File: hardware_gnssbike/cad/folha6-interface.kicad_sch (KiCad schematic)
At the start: 22 parts, among them Q601 DMG1012T-7, Q602 DMG1012T-7, Q603 DMG1012T-7, SW601 Omron B3S-1002P, SW602 Omron B3S-1002P, SW603 Omron B3S-1002P

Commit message: feat(hardware): the test points, a readable silkscreen, and paper that fits
Eleven of the sixteen test points of 06-conectores-e-pontos-de-teste.md were
not on the board. Only the three of the console sheet existed; a rail you
cannot put a probe on is a rail you cannot debug. VBUS, VBUSOUT, VBAT, VSYS,
3V0, 1V8, SD3V0, 3V3BL, VBCKP, VINT and the ground reference are there now,
each beside the thing it measures, and each takes what is LEFT: placed with
the rest of JUNTO they pushed three decoupling capacitors off their rings,
one of them to 4.0 mm from a pin that wants 2. The two that are still
missing are the document's own absences - TP111 measures ST_STO, which the
AEM10900 datasheet does not have, and TP401 measures 5V0, from a regulator
not fitted with the JDI panel. The list lives in parts.TESTE and nets.py
refuses a point that names a net that does not exist.

The silkscreen named nothing. Every reference sat 1.8 mm above its part at
0.7 mm with a 0.1 mm stroke - below the floor every fab publishes - and 37
pairs of designators printed on top of each other. The text is at the fab
minimum now, 0.8 mm with 0.15, and each label is PLACED: candidates around
its own courtyard, nearest first, never over another label and preferably
not over another part's outline. 127 references, 0 overlapping. The mounting
hole's REF** is hidden; it names nothing and was the last label sitting on
another.

Ground: a mesh, not just a hem. Edge stitching keeps the boundary of the
surface pours from becoming a radiating slot and does nothing for the
middle, where a patch of pour that reaches the inner plane through a via
20 mm away is not ground at 2.4 GHz. A 4.0 mm grid of ground vias now
covers the board - under the 6.1 mm that is a tenth of a wavelength in
FR-4 - laid last, on what is free, so a stitch never costs a connection.

The router's search learned about pad fields. The neck beside a pad existed
only in emitir(), and emitir only ever sees paths the search already found,
so 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
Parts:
- LS601: footprint Buzzer_Beeper:Buzzer_CUI_CPT-9019S-SMT -> gnssbike:Buzzer_CPT-1117-83-SMT_11x9mm
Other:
- moved on the sheet: C601, C602, C603, LS601, Q601, Q602, Q603, R601, R602, R603, R604, R605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

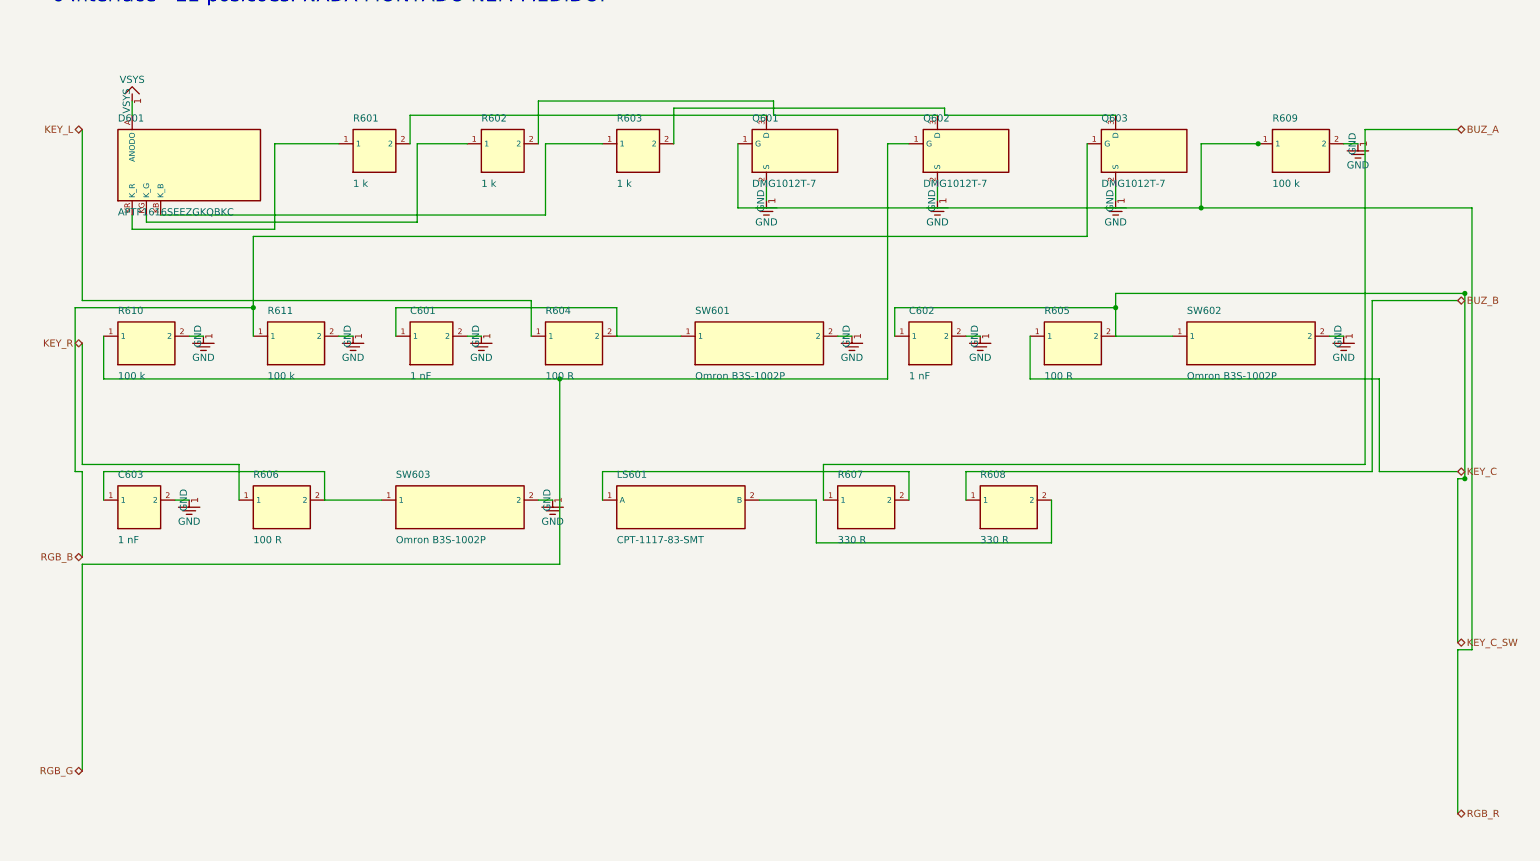
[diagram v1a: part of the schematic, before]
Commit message: feat(hardware): draw each part as its own symbol, not as a block
A rectangle with pin names down its sides is how an INTEGRATED CIRCUIT is
drawn, and only an integrated circuit. This generator drew all 127 parts
that way - resistors, ceramic capacitors, diodes, the TVS - and a sheet of
blocks joined by lines does not show a circuit.

Every class has its own symbol now, in the standard form, with the lead
axis on x and the body between -1.27 and +1.27 mm: a zigzag for a resistor
and a 0 ohm link (42 of them), two parallel plates for a ceramic capacitor
and a curved plate with a + for an electrolytic (31), four arcs for an
inductor (4), the same arcs inside a rectangle for a ferrite bead, which is
what tells the two apart, a zigzag with a diagonal arrow for the thermistor,
a triangle and a bar for a diode with arrows leaving it for an LED, two
contacts with a bar and a plunger for a key, a circle with a diagonal for
the buzzer, and a circle on the end of a lead for a test point. The 36 that
stay rectangles are the ones that should be: the ICs, the connectors and the
display. A two terminal part no longer prints pin numbers or pin names -
"1" and "2" on a resistor is noise, and the symbol already says which end is
which where it matters.

The power symbols had room reserved for the symbol and none for its NAME:
two ground pins two grid steps apart each got their own symbol, the symbols
did not collide, and the words printed over each other - "GNDGNDGND" along
the bottom of every chip. What is reserved now is the whole thing. With a
limit: the first cut let the stub run to fourteen grid steps looking for a
clear spot, and one of them crossed a component and split a net. A long stub
is worse than a crowded label, so it stops at eight and the label gives way.

One attempt is NOT in this commit, on purpose. Grouping every pin of a rail
on one edge into a single symbol - which is what a person draws - joins the
stubs with a line that runs along the part's edge and crosses w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
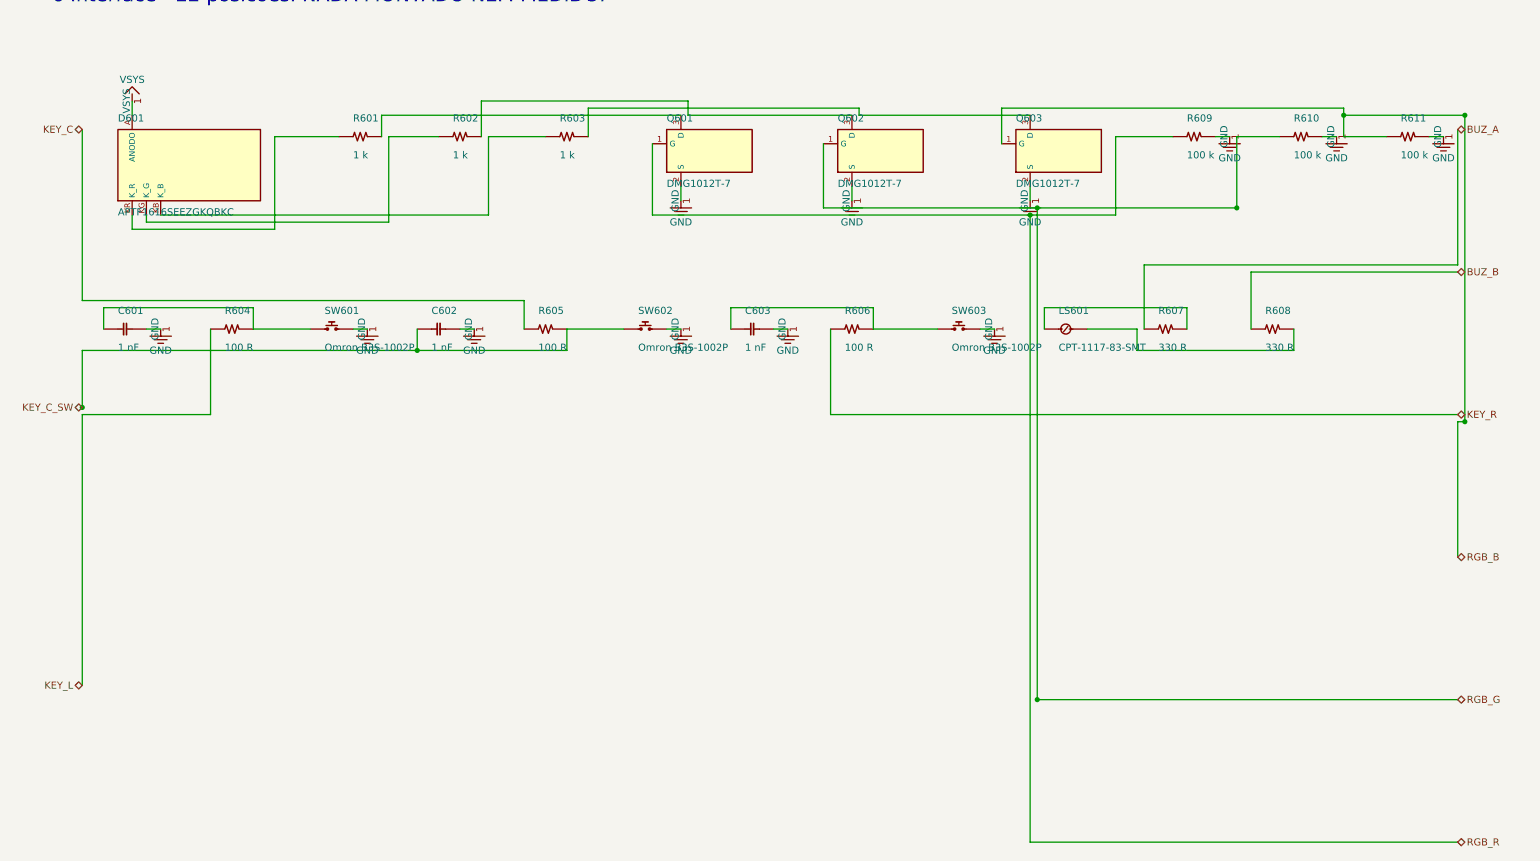
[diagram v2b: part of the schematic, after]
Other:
- moved on the sheet: Q601, Q602, Q603

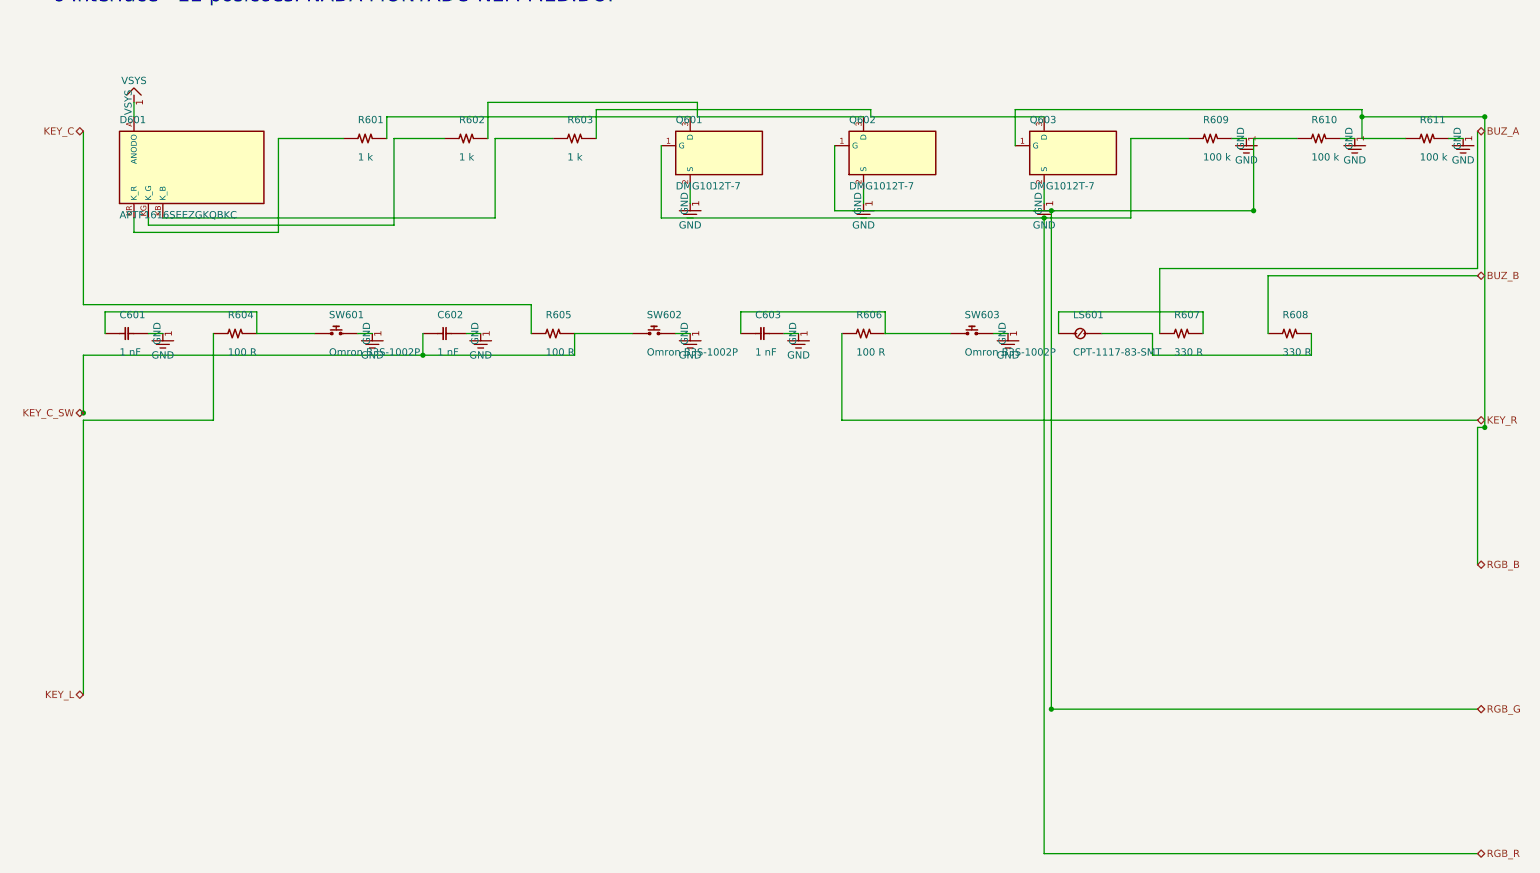
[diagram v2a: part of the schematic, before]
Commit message: feat(hardware): the four parts LCSC forced out, drawn from their drawings
The switch, the buzzer, the RGB LED and the magnetometer all had to
change, and each one came back from its drawing with something the
catalogue does not say.

  SW601..603  Omron B3S-1002P -> XunPu TS-1088R-02026 (C455280). It has
        TWO terminals, not four, so the land pattern is new even though
        the schematic already treated the key as two ends. Body 3,90 x
        3,00 x 2,00 against 6,6 x 6 x 3,4, which frees half the area the
        three keys took on the edge, and 260 gf against 230 - firmer,
        which is what gloves want. But the plunger rises only 0,50 mm
        above the steel cap against the Omron's 0,7, and the keys are
        pressed through the case: the case plunger changes.

  LS601  Same Sky CPT-1117-83-SMT (ONE in stock) -> Murata
        PKLCS1212E4001-R1 (C113159), the only substitute that keeps the
        84 dB. At 25 km/h with wind, the 65 to 70 dB of the 9 x 9 parts
        is inaudible, and an inaudible buzzer is no buzzer. The drawing
        corrects two things the catalogue hides: the sound hole is a
        LATERAL slot of 1,9 x 0,9 mm whose lower edge sits 0,30 mm off
        the board, with a channel underneath leaving by the opposite
        wall - so the case needs a side duct, not a hole in the lid -
        and the body is uniform dark graphite, with gold terminals, not
        black with a pale top. It also asks for 1 k to 2 k in series and
        forbids DC, which R607 and R608 now have to be checked against.

  D601  Kingbright APTF1616 (the suffix no longer exists, and what does
        has 305 pieces) -> TUOZHAN S4-3528RGBTA-A (C2827321), 2 million
        in stock at a twentieth of the price, common anode as the design
        wants. It is 3,5 x 2,8 instead of 1,6 x 1,6, so the LED zone had
        to widen and the part moved down 0,6 mm: at 1,9 mm tall it stood
        3,25 mm from the light sensor, which asks for twice a
        ne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
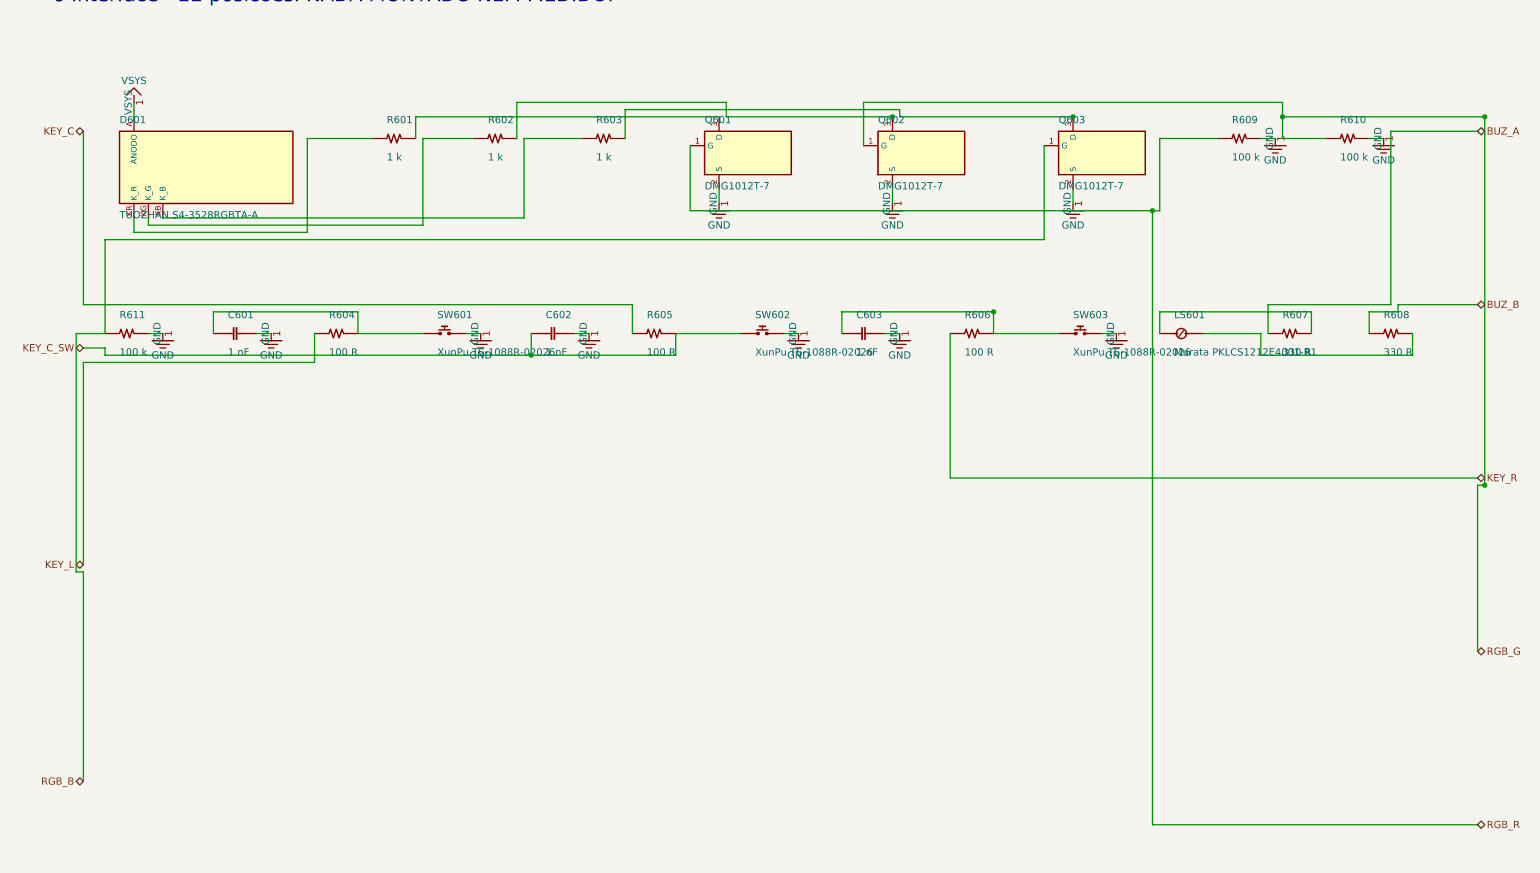
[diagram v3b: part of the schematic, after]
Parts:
- D601: value APTF1616SEEZGKQBKC -> TUOZHAN S4-3528RGBTA-A; footprint gnssbike:LED_RGB_APTF1616_1.6x1.6mm -> gnssbike:LED_RGB_3528_3.5x2.8mm
- LS601: value CPT-1117-83-SMT -> Murata PKLCS1212E4001-R1; footprint gnssbike:Buzzer_CPT-1117-83-SMT_11x9mm -> gnssbike:Buzzer_PKLCS1212E4001_12x12mm
- SW601, SW602, SW603: value Omron B3S-1002P -> XunPu TS-1088R-02026; footprint Button_Switch_SMD:SW_SPST_B3S-1000 -> gnssbike:SW_TS-1088R_3.9x3mm
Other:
- moved on the sheet: C601, C602, C603, D601, LS601, Q601, Q602, Q603, R601, R602, R603, R604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
